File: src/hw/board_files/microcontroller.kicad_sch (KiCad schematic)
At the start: 1 part, among them U4 MDBT50Q-1MV2

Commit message: Schematic progress
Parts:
- added U2: IS31FL3731-SA, Package_SO:SSOP-28_5.3x10.2mm_P0.65mm, symbol Driver_LED:IS31FL3731-SA
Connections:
- net MCU_USB_D-: now reaches U4.34 (D-)
- net MCU_USB_D+: now reaches U4.35 (D+)
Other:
- note added: "Microcontroller"
- moved on the sheet: U4
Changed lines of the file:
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@@
 		(company "B. Kuhn")
+	)
+	(text "Microcontroller"
+		(exclude_from_sim no)
+		(at 13.208 13.97 0)
+		(effects
+			(font
+				(size 3.81 3.81)
+				(thickness 0.762)
+				(bold yes)
+				(italic yes)
+			)
+			(justify left top)
+		)
+	)
+	(wire
+		(pts
+			(xy 91.44 95.25) (xy 101.6 95.25)
+		)
+		(stroke
+			(width 0)
+			(type default)
+		)
+	)
+	(wire
+		(pts
+			(xy 91.44 97.79) (xy 101.6 97.79)
+		)
+		(stroke
+			(width 0)
+			(type default)
+		)
+	)
+	(hierarchical_label "MCU_USB_D-"
+		(shape bidirectional)
+		(at 91.44 95.25 180)
+		(effects
+			(font
+				(size 1.27 1.27)
+			)
+			(justify right)
+		)
+	)
+	(hierarchical_label "MCU_USB_D+"
+		(shape bidirectional)
+		(at 91.44 97.79 180)
+		(effects
+			(font
+				(size 1.27 1.27)
+			)
+			(justify right)
+		)
 	)
 	(symbol
 		(lib_id "RF_Module:MDBT50Q-1MV2")
-		(at 142.24 96.52 0)
+		(at 121.92 95.25 0)
 		(unit 1)
 		(exclude_from_sim no)
@@
 		(fields_autoplaced yes)
 		(property "Reference" "U4"
-			(at 144.3833 142.24 0)
+			(at 124.0633 140.97 0)
 			(effects
 				(font
@@
 		)
 		(property "Value" "MDBT50Q-1MV2"
-			(at 144.3833 144.78 0)
+			(at 124.0633 143.51 0)
 			(effects
 				(font
@@
 		)
 		(property "Footprint" "RF_Module:Raytac_MDBT50Q"
-			(at 142.24 101.6 0)
+			(at 121.92 100.33 0)
 			(effects
 				(font
@@
 		)
 		(property "Datasheet" "https://www.raytac.com/download/index.php?index_id=43"
-			(at 142.24 101.6 0)
+			(at 121.92 100.33 0)
 			(effects
 				(font
@@
 		)
 		(property "Description" "Multiprotocol BLE/ANT/2.4 GHz/802.15.4 Cortex-M4F SoC, nRF52840 module"
-			(at 142.24 96.52 0)
+			(at 121.92 95.25 0)
 			(effects
 				(font
@@
 					(unit 1)
 				)
+			)
+		)
+	)
+	(symbol
+		(lib_id "Driver_LED:IS31FL3731-SA")
+		(at 223.52 86.36 0)
+		(unit 1)
+		(exclude_from_sim no)
+		(in_bom yes)
+		(on_board yes)
+		(dnp no)
+		(fields_autoplaced yes)
+		(property "Reference" "U2"
+			(at 225.6633 55.88 0)
+			(effects
+				(font
+					(size 1.27 1.27)
+				)
+				(justify left)
+			)
+		)
+		(property "Value" "IS31FL3731-SA"
+			(at 225.6633 58.42 0)
+			(effects
+				(font
+					(size 1.27 1.27)
+				)
+				(justify left)
+			)
+		)
+		(property "Footprint" "Package_SO:SSOP-28_5.3x10.2mm_P0.65mm"
+			(at 223.52 86.36 0)
+			(effects
+				(font
+					(size 1.27 1.27)
+				)
+				(hide yes)
+			)
+		)
+		(property "Datasheet" "http://www.issi.com/WW/pdf/31FL3731.pdf"
+			(at 223.52 86.36 0)
+			(effects
+				(font
+					(size 1.27 1.27)
+				)
+				(hide yes)
+			)
+		)
+		(property "Description" "9x16 LED matrix driver with 8-bit PWM and breathing, SSOP-28"
+			(at 223.52 86.36 0)
+			(effects
+				(font
+					(size 1.27 1.27)
+				)
+				(hide yes)
+			)
+		)
+		(pin "19"
+		)
+		(pin "6"
+		)
+		(pin "5"
+		)
+		(pin "23"
+		)
+		(pin "20"
+		)
+		(pin "18"
+		)
+		(pin "3"
+		)
+		(pin "4"
+		)
+		(pin "17"
+		)
+		(pin "16"
+		)
+		(pin "2"
+		)
+		(pin "21"
+		)
+		(pin "22"
+		)
+		(pin "24"
+		)
+		(pin "12"
+		)
+		(pin "27"
+		)
+		(pin "11"
+		)
+		(pin "25"
+		)
+		(pin "14"
+		)
+		(pin "13"
+		)
+		(pin "1"
+		)
+		(pin "9"
+		)
+		(pin "7"
+		)
+		(pin "8"
+		)
+		(pin "26"
+		)
+		(pin "28"
+		)
+		(pin "10"
+		)
+		(pin "15"
+		)
+		(instances
+			(project "keypad_usb_hub"
+				(path "/62136966-d911-451f-9518-a7827b282fe3/80eb8bed-550f-4706-a833-00f95ea5010a"
+					(reference "U2")
+					(unit 1)
+				)

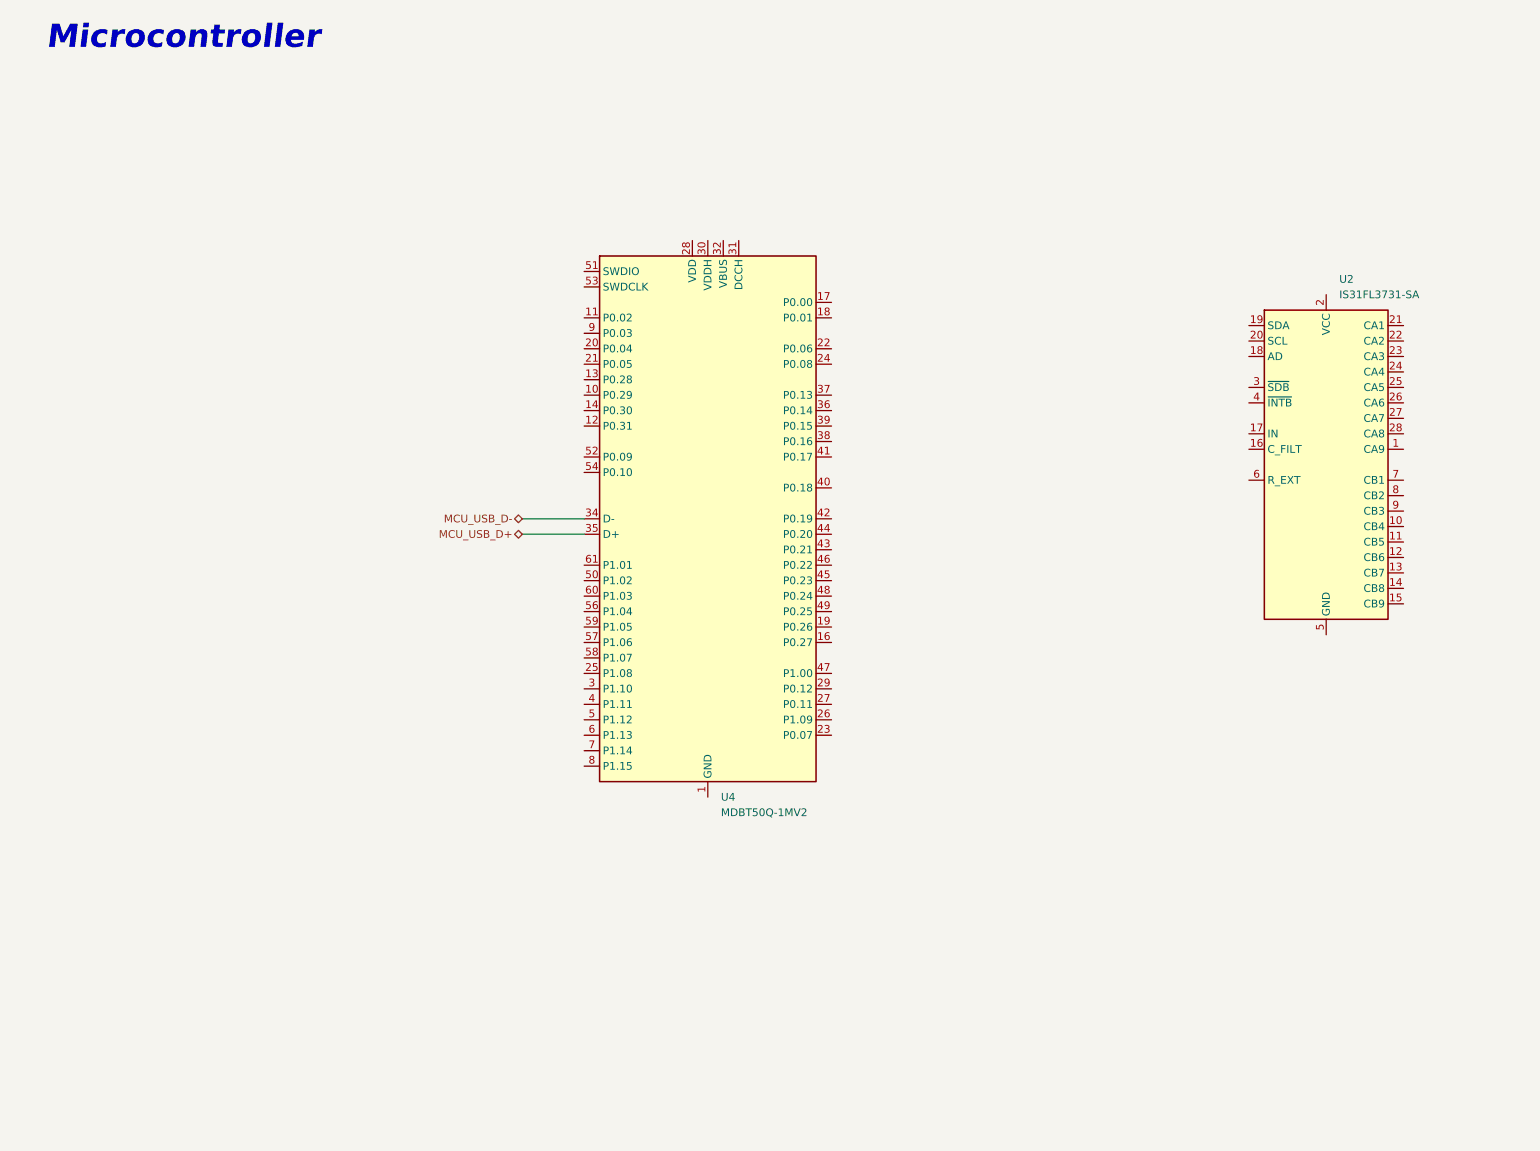
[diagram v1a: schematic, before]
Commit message: Finishing schematic. Need to review and clean up
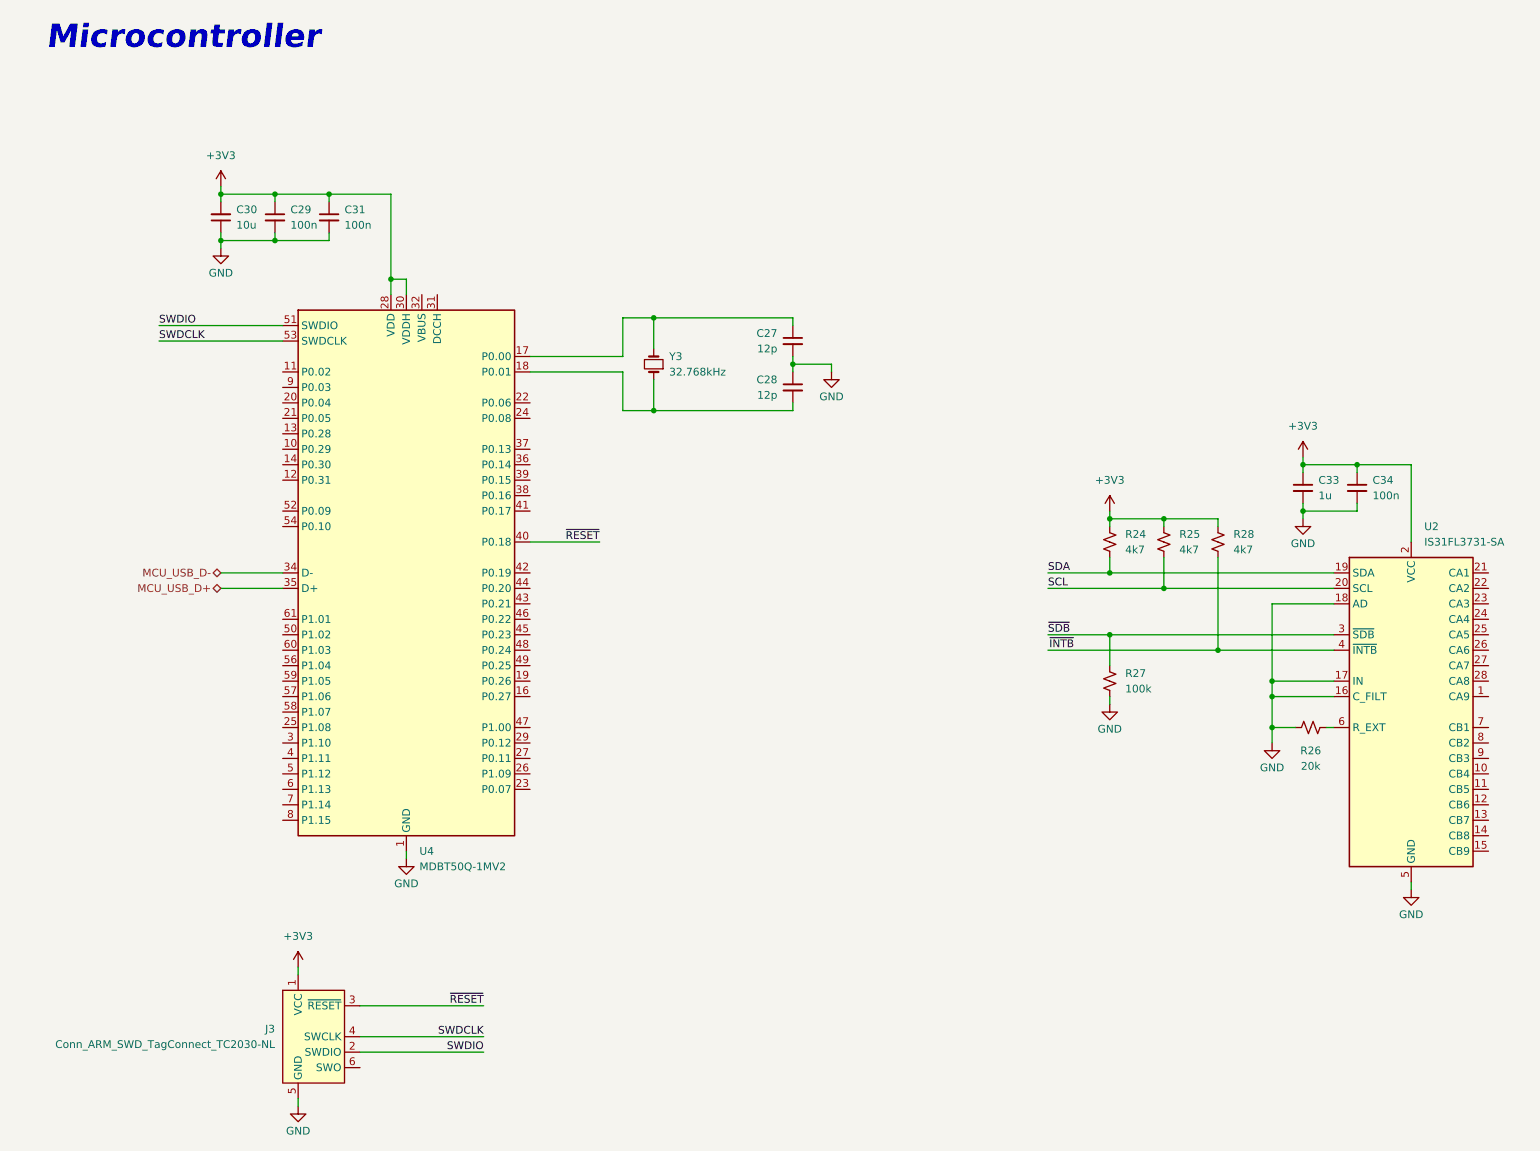
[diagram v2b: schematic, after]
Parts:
- added C27, C28: 12p, symbol Device:C_Small
- added C29, C31, C34: 100n, symbol Device:C_Small
- added C30: 10u, symbol Device:C_Small
- added C33: 1u, symbol Device:C_Small
- added J3: Conn_ARM_SWD_TagConnect_TC2030-NL, Connector:Tag-Connect_TC2030-IDC-NL_2x03_P1.27mm_Vertical, symbol Connector:Conn_ARM_SWD_TagConnect_TC2030-NL
- added R24, R25, R28: 4k7, symbol Device:R_Small_US
- added R26: 20k, symbol Device:R_Small_US
- added R27: 100k, symbol Device:R_Small_US
- added Y3: 32.768kHz, symbol Device:Crystal_Small
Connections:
- net GND: now reaches U4.1 (GND), U4.15 (GND), U4.2 (GND), U4.33 (GND), U4.55 (GND)
- net GND: now also U2.16 (C_FILT), U2.17 (IN), U2.18 (AD), U2.5 (GND), C27.2, C28.1, C29.2, C30.1, C31.2, C33.2, C34.2, J3.5 (GND), R26.1, R27.2
- net at U4.17 (P0.00): now also C27.1, Y3.2
- net at U4.18 (P0.01): now also C28.2, Y3.1
- net +3V3: now reaches U4.28 (VDD)
- net +3V3: now also U2.2 (VCC), U4.30 (VDDH), C29.1, C30.2, C31.1, C33.1, C34.1, J3.1 (VCC), R24.1, R25.1, R28.1
- net ~{RESET}: now reaches U4.40 (P0.18)
- net ~{RESET}: now also J3.3 (~{RESET})
- net SWDIO: now reaches U4.51 (SWDIO)
- net SWDIO: now also J3.2 (SWDIO)
- net SWDCLK: now reaches U4.53 (SWDCLK)
- net SWDCLK: now also J3.4 (SWCLK)
- net SDA: now reaches U2.19 (SDA)
- net SDA: now also R24.2
- net SCL: now reaches U2.20 (SCL)
- net SCL: now also R25.2
- net ~{SDB}: now reaches U2.3 (~{SDB})
- net ~{SDB}: now also R27.1
- net ~{INTB}: now reaches U2.4 (~{INTB})
- net ~{INTB}: now also R28.2
- net at U2.6 (R_EXT): now also R26.2
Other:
- moved on the sheet: U2, U4
